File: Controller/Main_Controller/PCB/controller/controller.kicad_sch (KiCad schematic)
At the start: 253 parts, among them J1 Conn_01x10, M1 Motor_DC, Q1 S9013, Q10 S9013, Q11 S9013, Q12 S9013, Q13 S9013, Q14 S9013, Q15 S9013, Q16 S9013, Q17 S9013, Q18 S9013, Q19 S9013, Q2 S9013, Q20 S9013, Q21 S9013, Q22 S9013, Q23 S9013, Q24 S9013, Q25 Q_PMOS_DGS, Q26 Q_NMOS_DGS, Q27 S9013, Q3 S9013, Q4 S9013, Q5 S9013, Q6 S9013, Q7 S9013, Q8 S9013, Q9 S9013, SW1 SW_SPDT, SW2 SW_SPDT, U1 NUCLEO-L432KC, U10 ZLDO1117G50TA, U2 NUCLEO144-F429ZI, U3 74HC14, U4 74HC14, U5 74HC14, U6 Joystick, U7 Joystick, U8 HY1602E, U9 ZSR330GTA

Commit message: Revert "Merge branch 'Controller' of https://github.com/LukeDWaller99/MEng-a-boys into Controller"
This reverts commit 01f8ef0eb2fb1fce7aa8fa9c8c27517fd2d5b7cd, reversing
changes made to d89a3e02795922979b099c1383eee3df5f29f7a2.
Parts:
- D12, D13, D5: value WHITE -> BLUE
- D14, D15, D16, D17, D19, D20, D22, D23, D24, D3, D4, D7, D8: value RED -> BLUE
- D18, D2, D6: value GREEN -> BLUE
- R11, R12, R15, R16, R30, R31, R32, R37, R39, R40, R46, R47, R48: value 150 -> 1K
- R13, R28, R29: value 390 -> 1K
- R14, R38, R4: value 2K2 -> 1K
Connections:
- net ASCEND_SB: no longer C6.2, D28.1 (K), R62.1, U3.9
- net BRAKE_MODE_SB: no longer C9.2, D31.1 (K), R65.1, U4.1
- net COL_SENS_1: now also R35.2
- net COL_SENS_3: now also U2.125 (PE15)
- net COL_SENS_7: now also U2.112 (PE8); no longer R35.2
- net DESCEND_SB: no longer C7.2, D29.1 (K), R63.1, U4.11
- net D_DOWN: now also U1.22 (A3)
- net D_LEFT_SB: now also C17.2, D37.1 (K), R81.1, U5.5
- net D_SELECT: now also U1.15 (D12)
- net D_SEL_SB: now also C19.2, D39.1 (K), R83.1, U5.11
- net D_UP: now also U1.19 (A0)
- net Earth: now also U1.6 (D3), U2.19 (GND), U2.20 (GND), U2.49 (GND), U2.8 (GND)
- net KILL_SWITCH_SB: no longer C5.2, D27.1 (K), R61.1, U3.5
- net LCD_D5: now also U1.8 (D5)
- net LIGHTS_SB: no longer C8.2, D30.1 (K), R64.1, U4.13
- net L_ROLL: now also U2.38 (PC0)
- net MOTOR_DENGAGE_SB: no longer C12.2, D34.1 (K), R68.1, U4.9
- net MOTOR_ENGAGE_SB: no longer C11.2, D33.1 (K), R67.1, U4.5
- net MOTOR_MODE_1: now also U2.52 (PF2)
- net MOTOR_MODE_1_SB: no longer C3.2, D25.1 (K), R59.1, U3.1
- net MOTOR_MODE_2_LED: now also U2.29 (PH0)
- net MOTOR_MODE_2_SB: no longer C4.2, D26.1 (K), R60.1, U3.3
- net REV_MODE_SB: no longer C10.2, D32.1 (K), R66.1, U4.3
- net SWITCH_1_SB: no longer C1.2, D9.1 (K), R19.1, U3.11
- net SWITCH_2_SB: no longer C2.2, D10.1 (K), R20.1, U3.13
- net MOTOR_DEN: now reaches U2.73 (PC9)
- new net: C11.2, D33.1 (K), R67.1, U4.5
- new net: C3.2, D25.1 (K), R59.1, U3.1
- new net: C4.2, D26.1 (K), R60.1, U3.3
- new net: C8.2, D30.1 (K), R64.1, U4.13
- new net: C5.2, D27.1 (K), R61.1, U3.5
- new net: C10.2, D32.1 (K), R66.1, U4.3
- new net: C2.2, D10.1 (K), R20.1, U3.13
- new net: C9.2, D31.1 (K), R65.1, U4.1
- new net: C12.2, D34.1 (K), R68.1, U4.9
- new net: C7.2, D29.1 (K), R63.1, U4.11
- new net: C1.2, D9.1 (K), R19.1, U3.11
- new net: C6.2, D28.1 (K), R62.1, U3.9
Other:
- moved on the sheet: C13, C14, C25, U5G

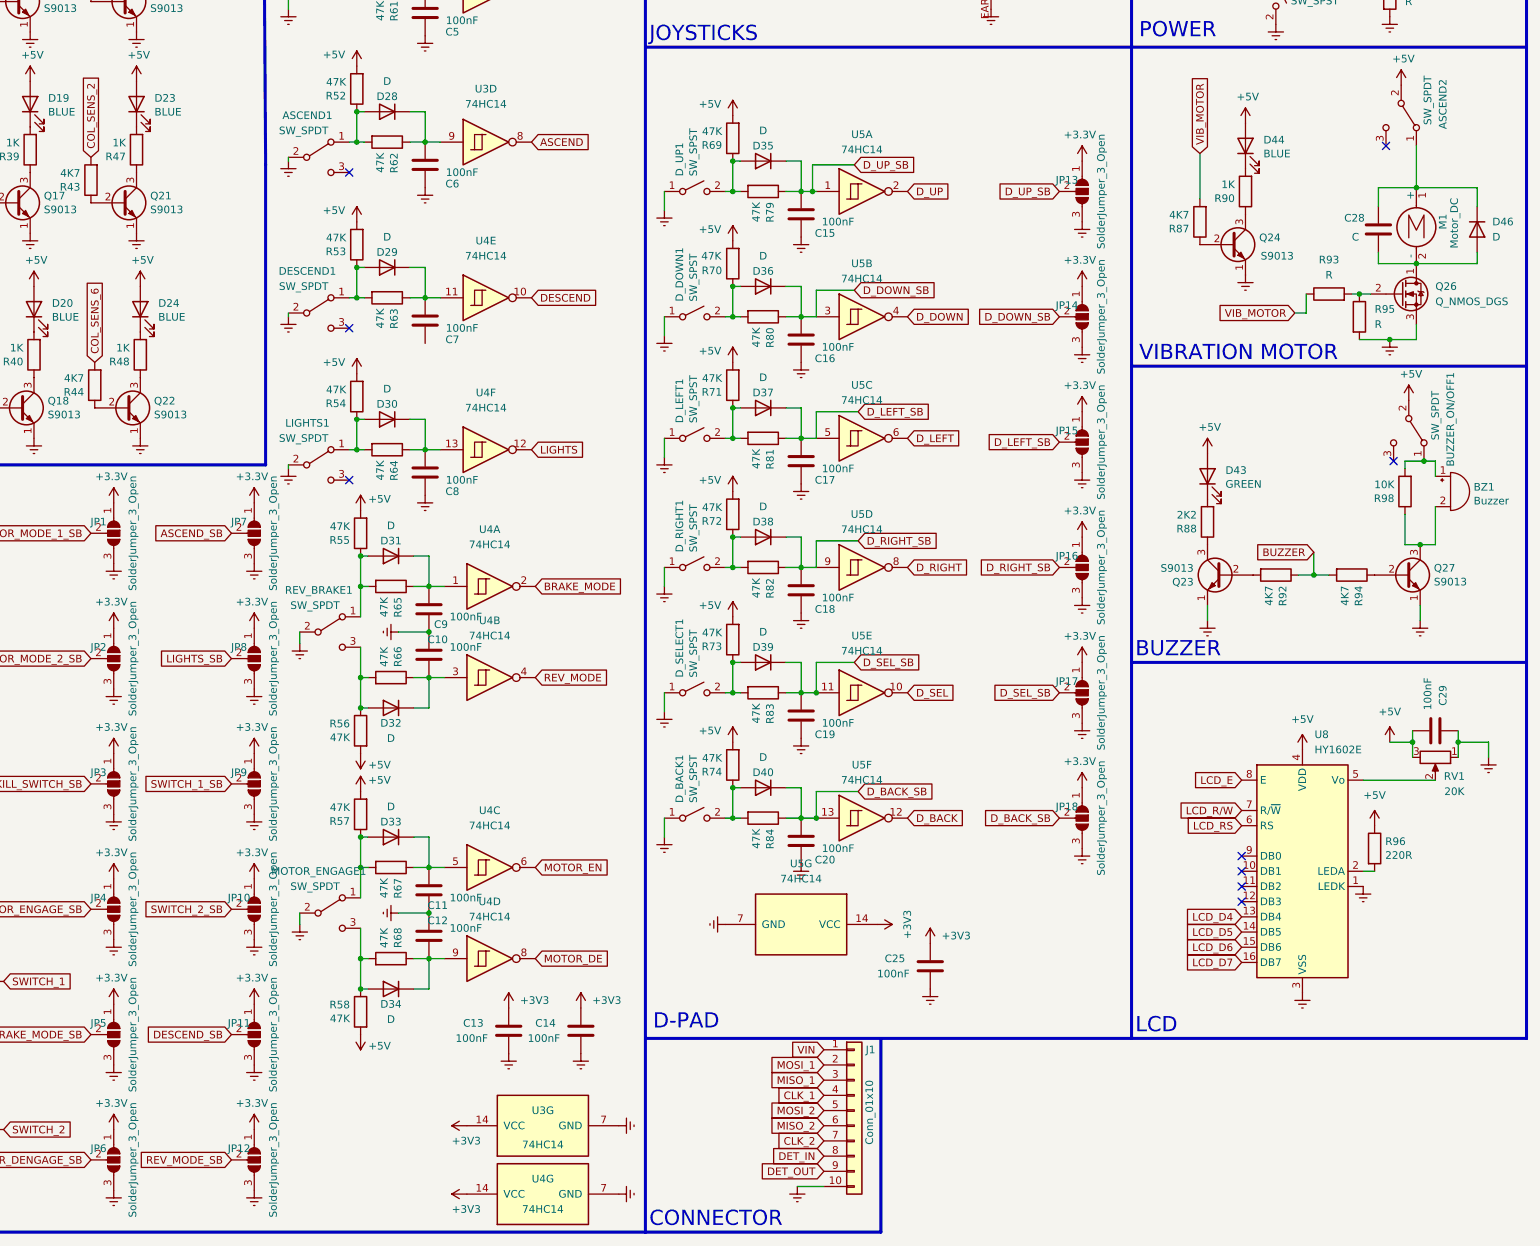
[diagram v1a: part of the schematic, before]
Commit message: Redesign ascend and descend switch.
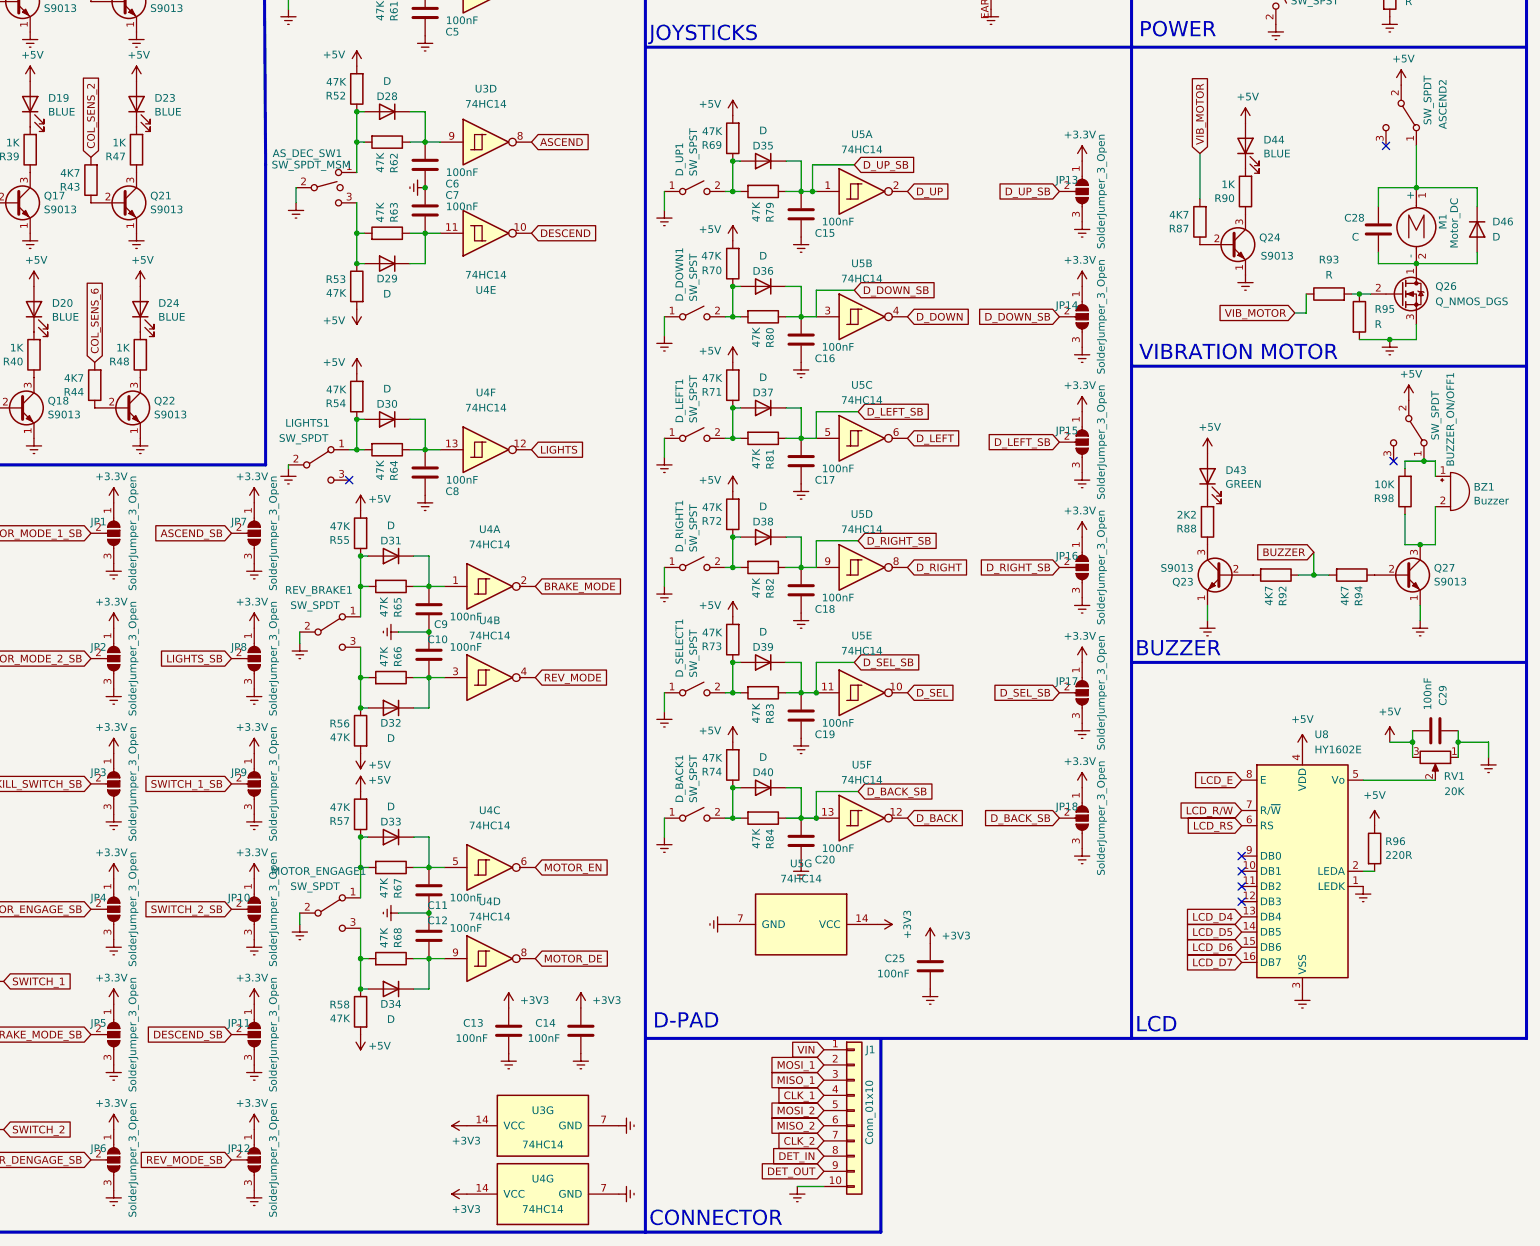
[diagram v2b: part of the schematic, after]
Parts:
- removed ASCEND1, DESCEND1: SW_SPDT, symbol Switch:SW_SPDT
- added AS_DEC_SW1: SW_SPDT_MSM, symbol Switch:SW_SPDT_MSM
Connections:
- net Earth: now also C7.1, AS_DEC_SW1.2
- net at D28.2 (A), R52.1, R62.2: now also AS_DEC_SW1.1
- net at D29.2 (A), R53.1, R63.2: now also AS_DEC_SW1.3
- no-connect marks 103 -> 101
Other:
- moved on the sheet: C7, D29, R53, R63, U4E

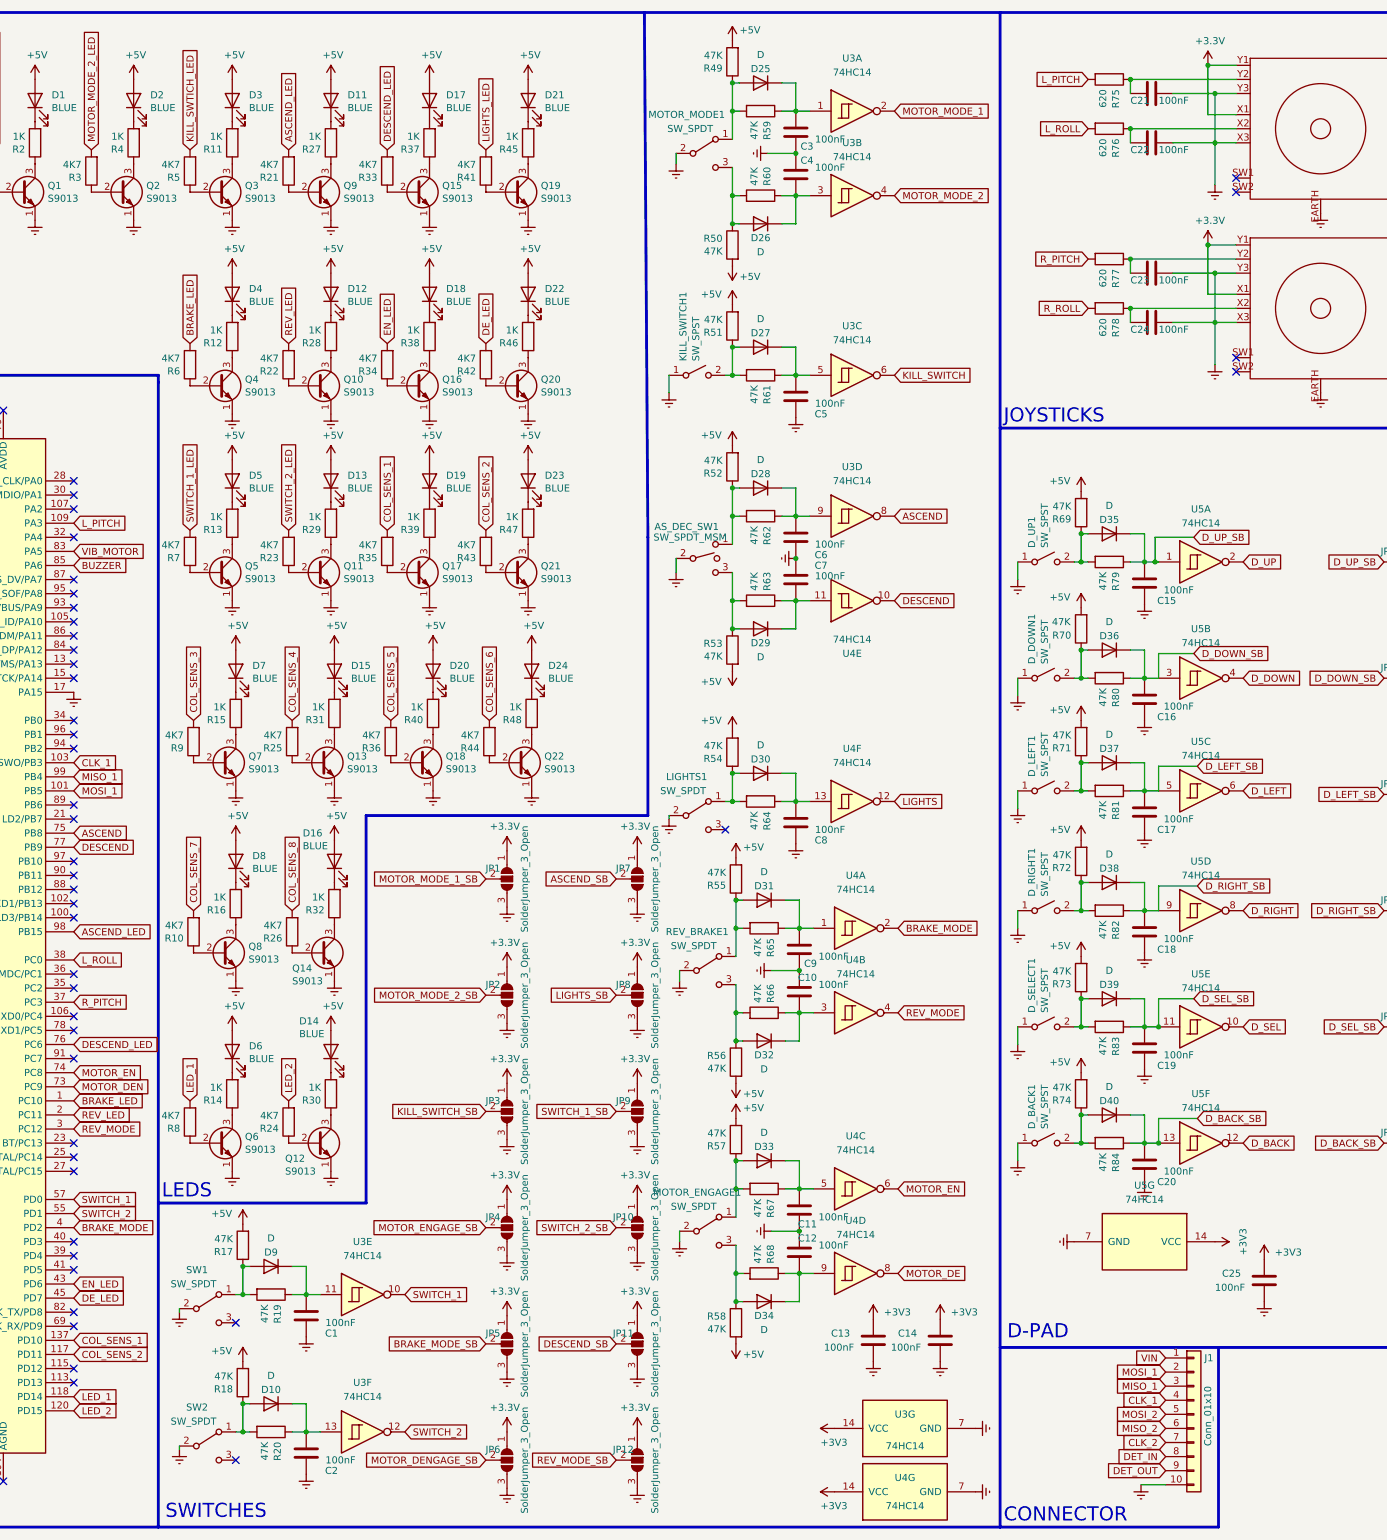
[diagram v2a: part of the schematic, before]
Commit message: Solder bridge connections and LED colours.
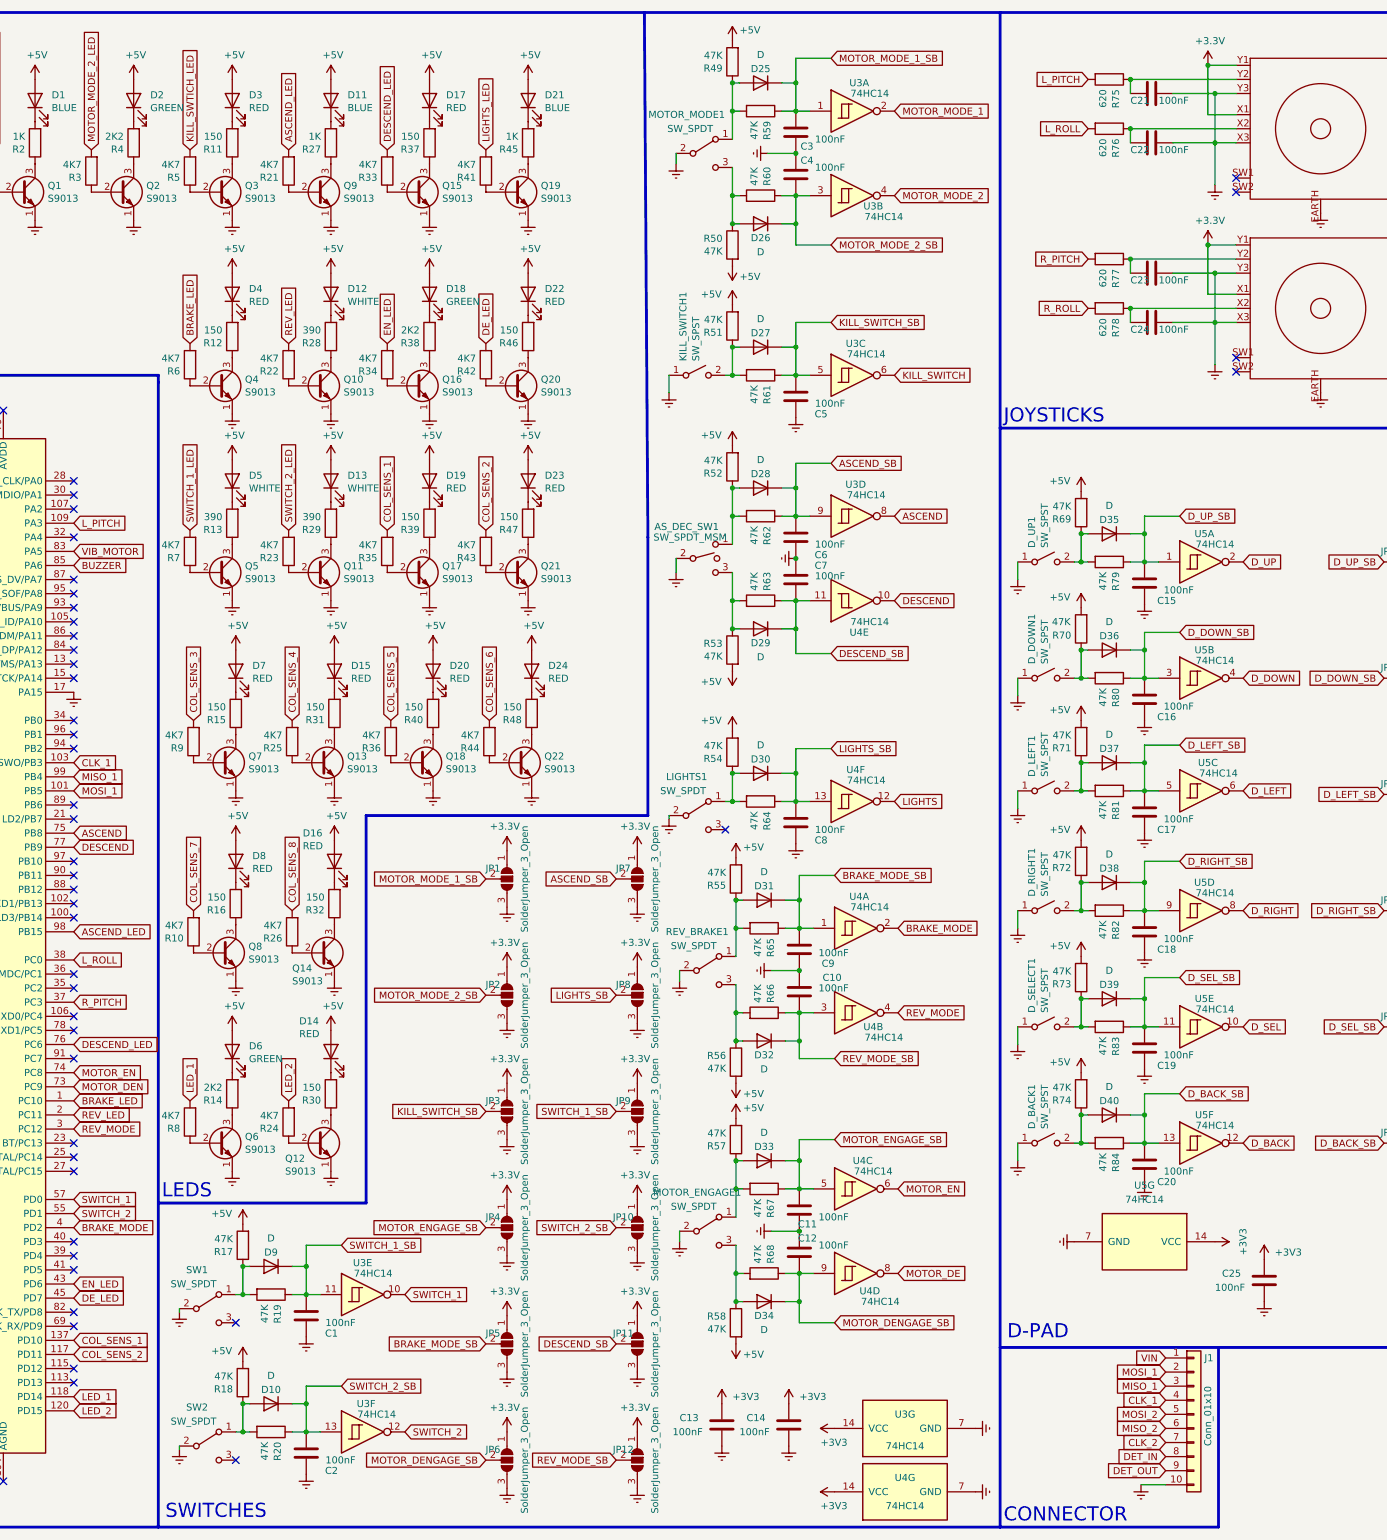
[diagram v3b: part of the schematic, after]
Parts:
- D12, D13, D5: value BLUE -> WHITE
- D14, D15, D16, D17, D19, D20, D22, D23, D24, D3, D4, D7, D8: value BLUE -> RED
- D18, D2, D6: value BLUE -> GREEN
- R11, R12, R15, R16, R30, R31, R32, R37, R39, R40, R46, R47, R48: value 1K -> 150
- R13, R28, R29: value 1K -> 390
- R14, R38, R4: value 1K -> 2K2
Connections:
- net ASCEND_SB: now also C6.2, D28.1 (K), R62.1, U3.9
- net BRAKE_MODE_SB: now also C9.2, D31.1 (K), R65.1, U4.1
- net DESCEND_SB: now also C7.2, D29.1 (K), R63.1, U4.11
- net KILL_SWITCH_SB: now also C5.2, D27.1 (K), R61.1, U3.5
- net LIGHTS_SB: now also C8.2, D30.1 (K), R64.1, U4.13
- net MOTOR_DENGAGE_SB: now also C12.2, D34.1 (K), R68.1, U4.9
- net MOTOR_ENGAGE_SB: now also C11.2, D33.1 (K), R67.1, U4.5
- net MOTOR_MODE_1_SB: now also C3.2, D25.1 (K), R59.1, U3.1
- net MOTOR_MODE_2_SB: now also C4.2, D26.1 (K), R60.1, U3.3
- net REV_MODE_SB: now also C10.2, D32.1 (K), R66.1, U4.3
- net SWITCH_1_SB: now also C1.2, D9.1 (K), R19.1, U3.11
- net SWITCH_2_SB: now also C2.2, D10.1 (K), R20.1, U3.13
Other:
- moved on the sheet: C13, C14
